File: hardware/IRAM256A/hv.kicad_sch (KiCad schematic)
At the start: 21 parts

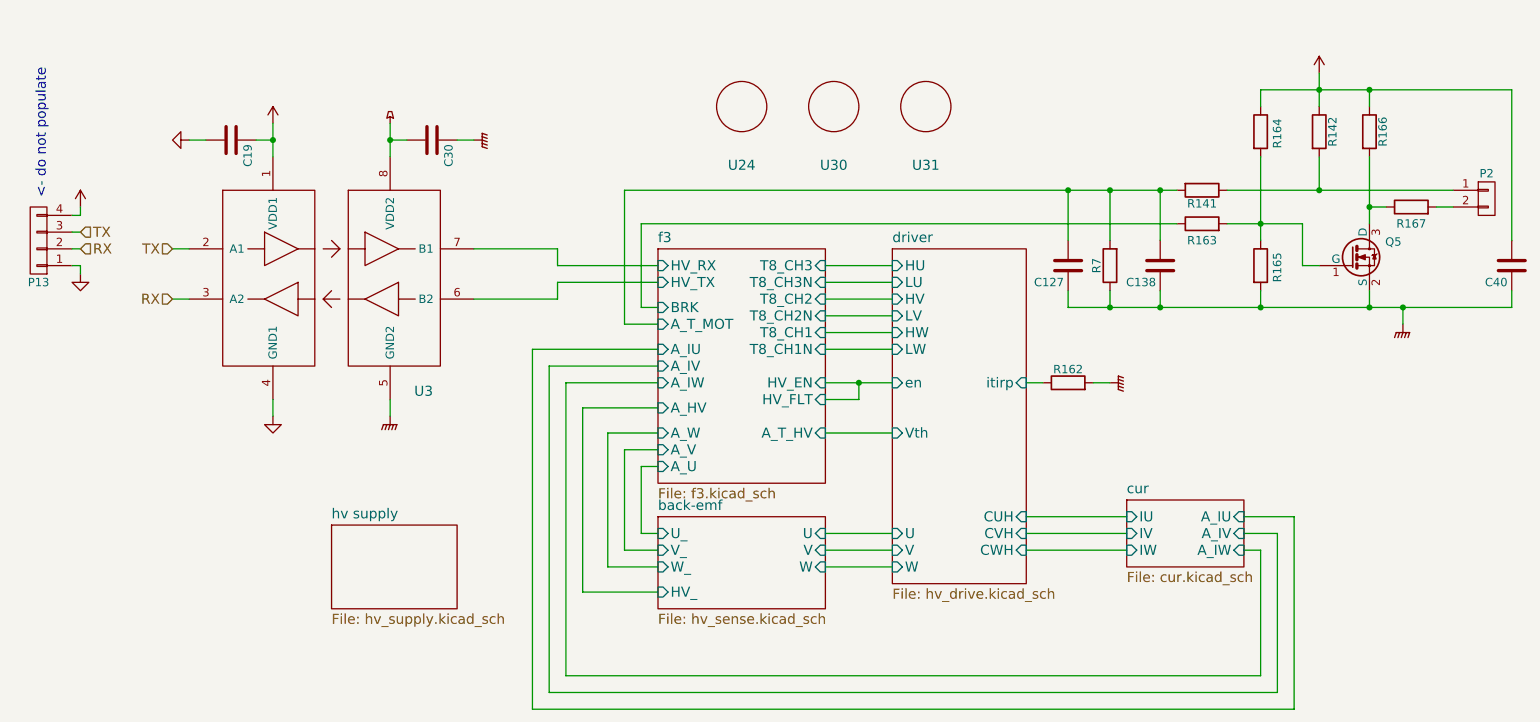
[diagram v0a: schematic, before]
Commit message: Structure change + kicad 3d models updated
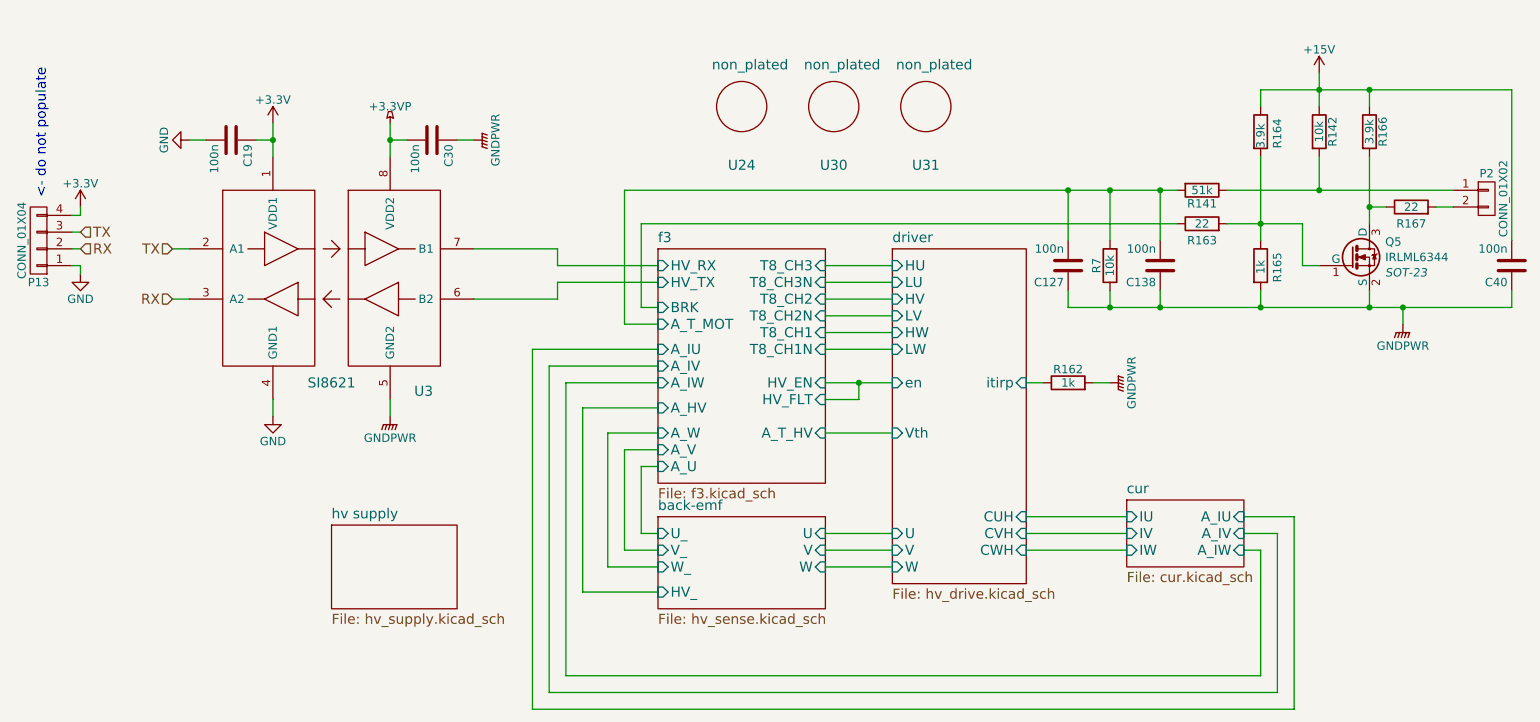
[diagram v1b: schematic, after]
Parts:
- C127, C138, C19, C30, C40: value (none) -> 100n; footprint (none) -> stmbl:C_0603
- P13: value (none) -> CONN_01X04; footprint (none) -> stmbl:Socket_Strip_Straight_1x04
- P2: value (none) -> CONN_01X02; footprint (none) -> stmbl:RM3.5_1x2
- Q5: value (none) -> IRLML6344; footprint (none) -> SOT-23
- R141: value (none) -> 51k; footprint (none) -> stmbl:R_0603
- R142, R7: value (none) -> 10k; footprint (none) -> stmbl:R_0603
- R162, R165: value (none) -> 1k; footprint (none) -> stmbl:R_0603
- R163, R167: value (none) -> 22; footprint (none) -> stmbl:R_0603
- R164, R166: value (none) -> 3.9k; footprint (none) -> stmbl:R_0603
- U24, U30, U31: value (none) -> non_plated; footprint (none) -> stmbl:non_plated_3mm
- U3: value (none) -> SI8621; footprint (none) -> stmbl:SOIC-8-N
